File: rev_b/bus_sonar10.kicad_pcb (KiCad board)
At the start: 2 copper layers, 100 x 50 mm, 36 parts, among them J1 TERMINATE_JUMPER, SW1 MJTP1243, U1 74HCT08, U2 LM2940, U3 MCP2562, U4 ATMEGA328_DIP28, U5 74HCT32, X1 CRYSTAL

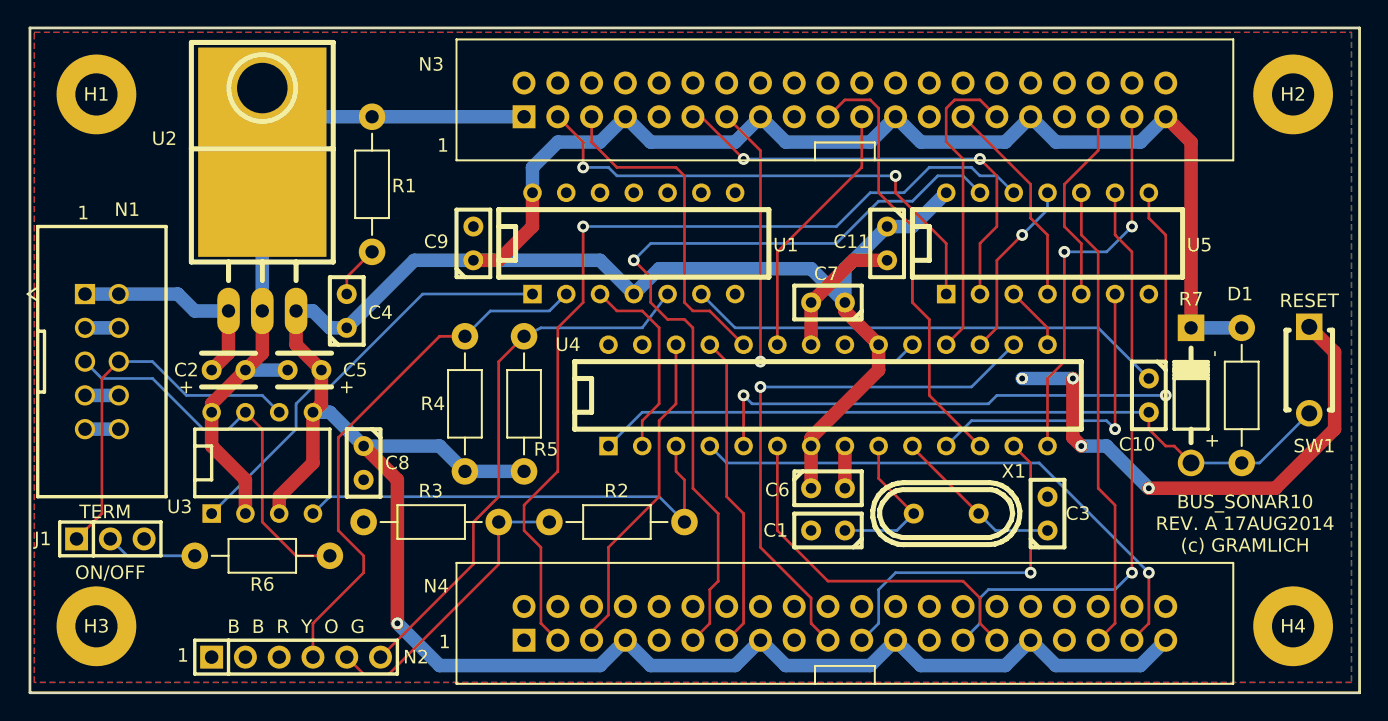
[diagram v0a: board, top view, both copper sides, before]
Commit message: Imported the new network into Rev. B.
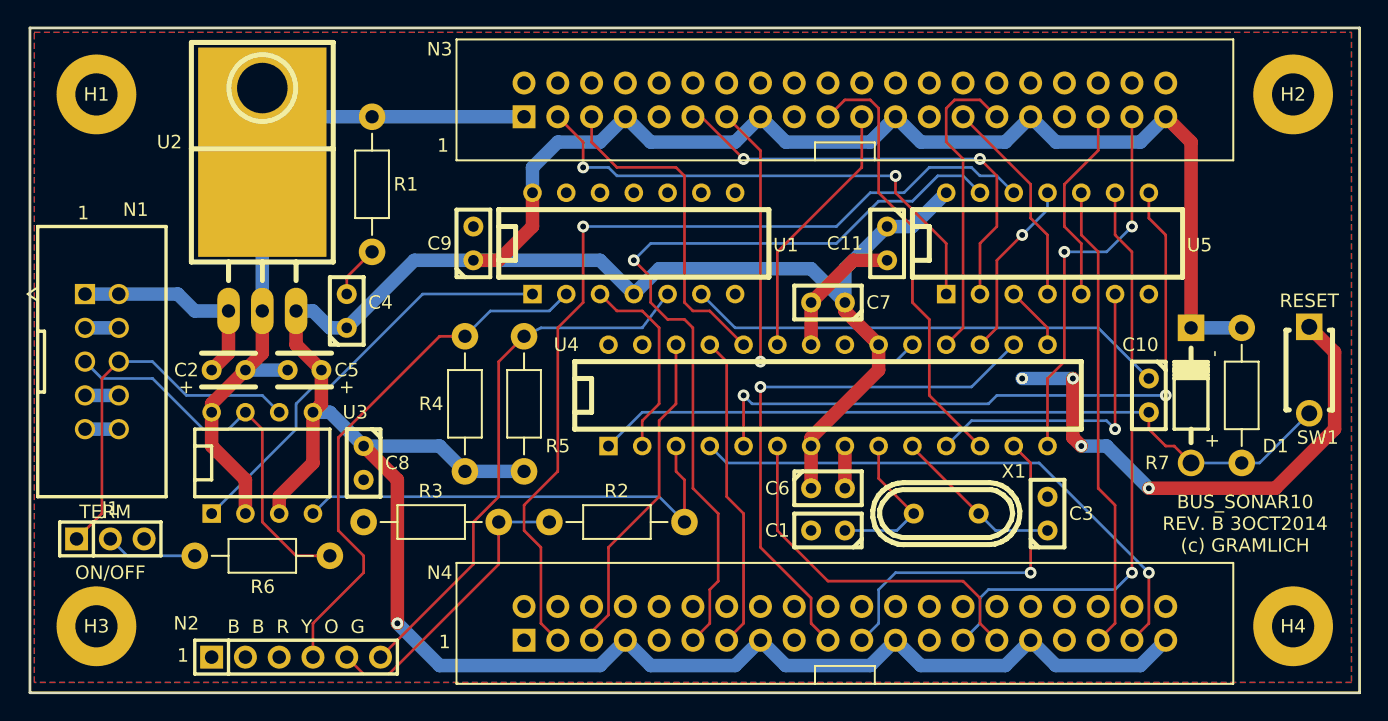
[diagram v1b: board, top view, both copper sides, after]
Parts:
- C1, C10, C11, C3, C4, C6, C7, C8, C9: footprint Bus_Sonar10_Rev_A:Capacitor3MMDiscRM2.5 -> bus_sonar10:Capacitor3MMDiscRM2.5
- C2, C5: footprint Bus_Sonar10_Rev_A:Capacitor4x3RM2-5_RevB -> bus_sonar10:Capacitor4x3RM2-5_RevB
- D1: footprint Bus_Sonar10_Rev_A:Diode_DO-41_SOD81_Horizontal_RM10 -> bus_sonar10:Diode_DO-41_SOD81_Horizontal_RM10
- G1: footprint Bus_Sonar10_Rev_A:OSHW_LOGO_400mil -> bus_sonar10:OSHW_LOGO_400mil
- H1, H2, H3, H4: footprint Bus_Sonar10_Rev_A:MountingHole_3mm -> bus_sonar10:MountingHole_3mm
- J1: footprint Bus_Sonar10_Rev_A:Pin_Header_Straight_1x03 -> bus_sonar10:Pin_Header_Straight_1x03
- N1: footprint Bus_Sonar10_Rev_A:Pin_Header_Straight_2x05_Shrouded -> bus_sonar10:Pin_Header_Straight_2x05_Shrouded
- N2: footprint Bus_Sonar10_Rev_A:Pin_Header_Straight_1x06 -> bus_sonar10:Pin_Header_Straight_1x06
- N3, N4: footprint Bus_Sonar10_Rev_A:Pin_Header_Straight_2x20_Shrouded -> bus_sonar10:Pin_Header_Straight_2x20_Shrouded
- R1, R2, R3, R4, R5, R6, R7: footprint Bus_Sonar10_Rev_A:Resistor_Horizontal_400 -> bus_sonar10:Resistor_Horizontal_400
- SW1: footprint Bus_Sonar10_Rev_A:Button_6.5MM -> bus_sonar10:Button_6.5MM
- U1, U5: footprint Bus_Sonar10_Rev_A:DIP-14__300 -> bus_sonar10:DIP-14__300
- U2: footprint Bus_Sonar10_Rev_A:TO-220_Neutral123_Horizontal_LargePads -> bus_sonar10:TO-220_Neutral123_Horizontal_LargePads
- U3: footprint Bus_Sonar10_Rev_A:DIP-8__300 -> bus_sonar10:DIP-8__300
- U4: footprint Bus_Sonar10_Rev_A:DIP-28__300 -> bus_sonar10:DIP-28__300
- X1: value CRYSTAL -> 16MHz; footprint Bus_Sonar10_Rev_A:Crystal_HC49-U_Vertical -> bus_sonar10:Crystal_HC49-U_Vertical
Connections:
- J1 pad 3: Net-(J1-Pad3) -> (no net)
- N2 pad 2: Net-(N2-Pad2) -> (no net)
- N2 pad 3: Net-(N2-Pad3) -> (no net)
- U4 pad 21: Net-(U4-Pad21) -> (no net)
- U4 pad 27: Net-(U4-Pad27) -> (no net)
- U4 pad 28: Net-(U4-Pad28) -> (no net)
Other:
- board text added: "BUS_SONAR10 REV. B 3OCT2014 (c) GRAMLICH"
- board text removed: "BUS_SONAR10 REV. A 17AUG2014 (c) GRAMLICH"

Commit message: Got Rev. B in pretty good shape.
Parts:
- added D2: LED, bus_sonar10:T1_LED, F.Cu at (128.3, 125.7)
- added R8: 100K, bus_sonar10:Resistor_Horizontal_400, F.Cu at (117.5, 142.9)
- added R9: 470, bus_sonar10:Resistor_Horizontal_400, F.Cu at (130.2, 116.2)
- moved R4 0.63 mm to (133.3, 128.3)
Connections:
- U1 pad 1: Net-(U1-Pad1) -> /CAN_RXD
- U1 pad 10: (no net) -> Net-(U1-Pad10)
- U1 pad 11: (no net) -> Net-(U1-Pad10)
- U1 pad 12: (no net) -> +5V
- U1 pad 13: (no net) -> +5V
- U1 pad 9: (no net) -> Net-(U1-Pad10)
- U3 pad 1: Net-(U1-Pad1) -> /TXD
- U3 pad 4: /TXD -> /CAN_RXD
- U3 pad 8: GND -> Net-(U3-Pad8)
- U4 pad 27: (no net) -> Net-(R9-Pad1)
- U4 pad 28: (no net) -> Net-(U3-Pad8)
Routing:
- net /CAN_RXD: track 0.00 -> 36.9 mm, vias 0 -> 1
- net Net-(U1-Pad1): track 32.1 -> 0.00 mm
- net Net-(U3-Pad8): track 0.00 -> 31.9 mm, vias 0 -> 1
- net GND: track 116.5 -> 142.7 mm
- net Net-(R9-Pad1): track 0.00 -> 26.0 mm, vias 0 -> 1
- net +5V: track 278.7 -> 292.0 mm
- net /TXD: track 35.2 -> 45.0 mm
- net Net-(U1-Pad10): track 0.00 -> 5.08 mm
- net Net-(D2-Pad+): track 0.00 -> 3.96 mm
- net /RXD: track 14.9 -> 12.7 mm
- net Net-(N2-Pad4): track 40.5 -> 42.0 mm
